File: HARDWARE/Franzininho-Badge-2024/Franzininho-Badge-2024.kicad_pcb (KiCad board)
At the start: 2 copper layers, 96 x 64 mm, 15 parts, among them SW1 SW_Push, U1 CH32V003F4P6

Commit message: Esboço inicial do layout.
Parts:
- added C4: 100nF, Capacitor_SMD:C_0603_1608Metric_Pad1.08x0.95mm_HandSolder, F.Cu at (112.1, 88.5)
- added C5: 10uF, Capacitor_SMD:C_0805_2012Metric_Pad1.18x1.45mm_HandSolder, F.Cu at (128.9, 81.7)
- added C6: 100nF, Capacitor_SMD:C_0603_1608Metric_Pad1.08x0.95mm_HandSolder, F.Cu at (128.7, 84.5)
- added J1: Conn_01x03_Pin, Connector_PinHeader_2.54mm:PinHeader_1x03_P2.54mm_Horizontal, F.Cu at (177.2, 105.4)
- added J2: Conn_01x04_Pin, Connector_PinHeader_2.54mm:PinHeader_1x04_P2.54mm_Horizontal, F.Cu at (177.2, 92.7)
- added R10: 1K, Resistor_SMD:R_0603_1608Metric_Pad0.98x0.95mm_HandSolder, F.Cu at (145.5, 105.4)
- added R11: 1K, Resistor_SMD:R_0603_1608Metric_Pad0.98x0.95mm_HandSolder, F.Cu at (128.5, 97.3)
- added R12: 1K, Resistor_SMD:R_0603_1608Metric_Pad0.98x0.95mm_HandSolder, F.Cu at (128.5, 98.8)
- added R13: 1K, Resistor_SMD:R_0603_1608Metric_Pad0.98x0.95mm_HandSolder, F.Cu at (145.5, 103.9)
- added R3: 1K, Resistor_SMD:R_0603_1608Metric_Pad0.98x0.95mm_HandSolder, F.Cu at (131.8, 97.3)
- added R4: 1K, Resistor_SMD:R_0603_1608Metric_Pad0.98x0.95mm_HandSolder, F.Cu at (131.8, 98.8)
- added R5: 1K, Resistor_SMD:R_0603_1608Metric_Pad0.98x0.95mm_HandSolder, F.Cu at (131.8, 100.8)
- added R6: 1K, Resistor_SMD:R_0603_1608Metric_Pad0.98x0.95mm_HandSolder, F.Cu at (131.8, 102.4)
- added R7: 1K, Resistor_SMD:R_0603_1608Metric_Pad0.98x0.95mm_HandSolder, F.Cu at (131.8, 103.9)
- added R8: 1K, Resistor_SMD:R_0603_1608Metric_Pad0.98x0.95mm_HandSolder, F.Cu at (131.8, 105.4)
- added R9: 1K, Resistor_SMD:R_0603_1608Metric_Pad0.98x0.95mm_HandSolder, F.Cu at (131.8, 106.9)
- added U2: OLED 128x64 1.3", Franzininho-Badge:OLED 128x64 1.3in, B.Cu at (139.7, 88.9)
- added U3: ~, Franzininho-Badge:EPAPER_1.54in_200x200, B.Cu at (139.7, 101.6)
- moved C2 15.4 mm to (146.3, 100.0), turned to -90 degrees
- moved C3 11.7 mm to (144.5, 100.0), turned to 90 degrees
- moved U1 1.63 mm to (139.7, 101.6), turned to 180 degrees
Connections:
- U1 pad 1: unconnected-(U1-PD4-Pad1) -> Net-(U1-PD4)
- U1 pad 11: unconnected-(U1-PC1-Pad11) -> Net-(U1-PC1)
- U1 pad 12: unconnected-(U1-PC2-Pad12) -> Net-(U1-PC2)
- U1 pad 15: unconnected-(U1-PC5-Pad15) -> Net-(U1-PC5)
- U1 pad 16: unconnected-(U1-PC6-Pad16) -> Net-(U1-PC6)
- U1 pad 18: unconnected-(U1-PD1-Pad18) -> Net-(U1-PD1)
- U1 pad 19: unconnected-(U1-PD2-Pad19) -> Net-(U1-PD2)
- U1 pad 2: unconnected-(U1-PD5-Pad2) -> Net-(U1-PD5)
- U1 pad 20: unconnected-(U1-PD3-Pad20) -> Net-(U1-PD3)
- U1 pad 3: unconnected-(U1-PD6-Pad3) -> MCU RX
- U1 pad 8: unconnected-(U1-PD0-Pad8) -> EPD BUSY
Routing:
- net SWIO: track 0.00 -> 48.1 mm
- net EPD BUSY: track 0.00 -> 41.8 mm
- net MCU RX: track 0.00 -> 37.9 mm
- net MCU TX: track 0.00 -> 33.2 mm
- net EPD RES: track 0.00 -> 24.3 mm
- net EPD D/C: track 0.00 -> 21.5 mm
- net SPI SCK: track 0.00 -> 15.6 mm
- net I2C SCL: track 0.00 -> 14.9 mm
- net SPI MOSI: track 0.00 -> 12.4 mm
- net I2C SDA: track 0.00 -> 11.9 mm
- net Net-(U1-PD3): track 0.00 -> 5.10 mm
- net Net-(U1-PD2): track 0.00 -> 4.73 mm
- net Net-(U1-PC1): track 0.00 -> 4.68 mm
- net Net-(U1-PD1): track 0.00 -> 4.37 mm
- net Net-(U1-PC2): track 0.00 -> 4.31 mm
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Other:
- board text added: "FRANZININHO BADGE 2024"

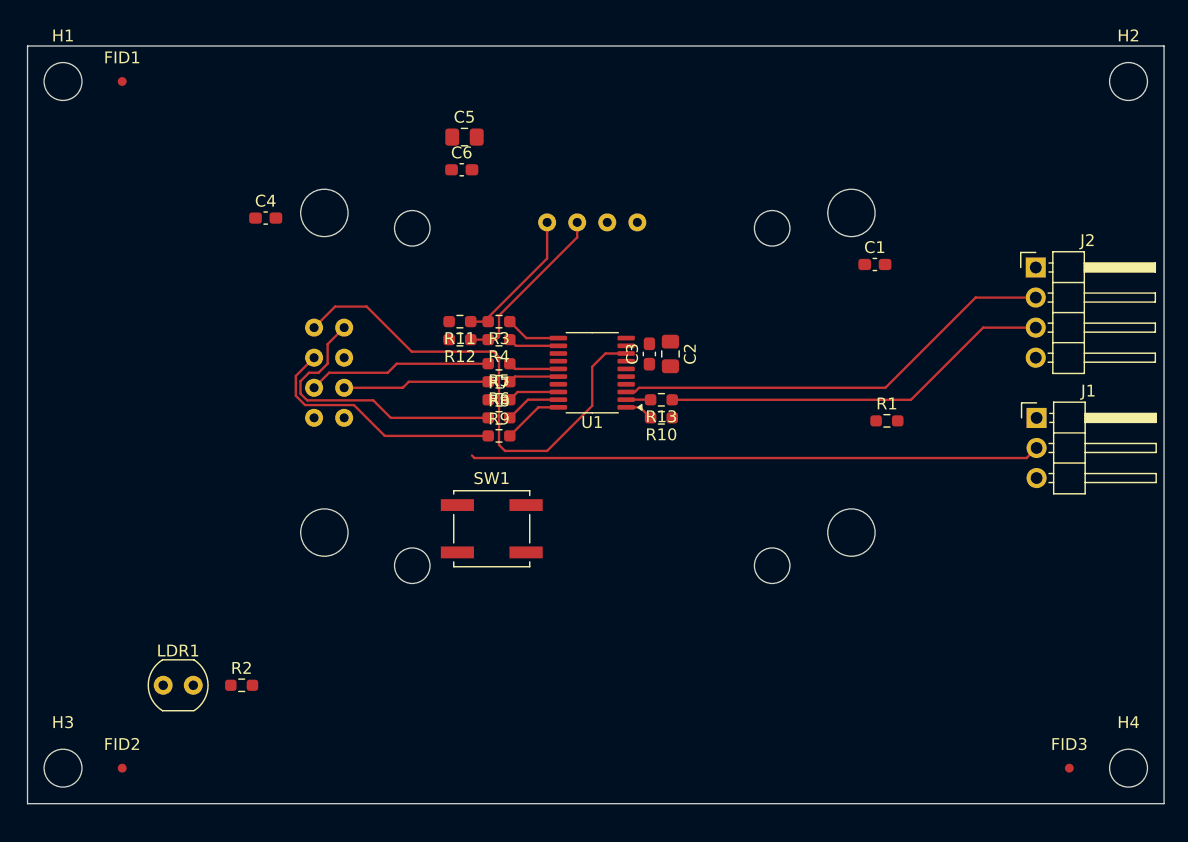
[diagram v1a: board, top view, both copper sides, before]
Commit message: Adicionado display de 2.13in; continuação do layout.
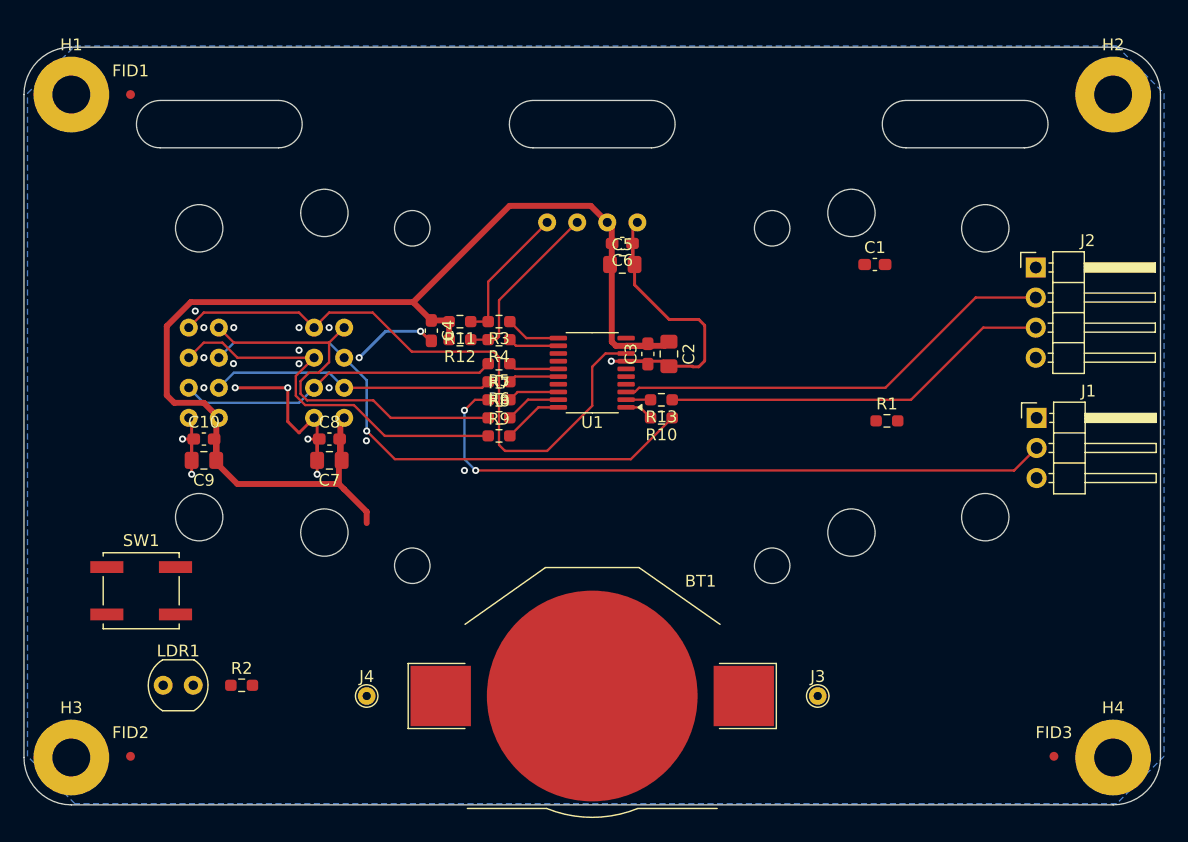
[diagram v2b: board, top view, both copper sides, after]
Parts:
- added BT1: CR2032, Battery:BatteryHolder_Keystone_3002_1x2032, F.Cu at (139.7, 128.9)
- added C10: 100nF, Capacitor_SMD:C_0603_1608Metric_Pad1.08x0.95mm_HandSolder, F.Cu at (106.9, 107.2)
- added C7: 10uF, Capacitor_SMD:C_0805_2012Metric_Pad1.18x1.45mm_HandSolder, F.Cu at (117.5, 109.0)
- added C8: 100nF, Capacitor_SMD:C_0603_1608Metric_Pad1.08x0.95mm_HandSolder, F.Cu at (117.5, 107.2)
- added C9: 10uF, Capacitor_SMD:C_0805_2012Metric_Pad1.18x1.45mm_HandSolder, F.Cu at (106.9, 109.0)
- added J3: +3V3, TestPoint:TestPoint_THTPad_D1.5mm_Drill0.7mm, F.Cu at (158.8, 128.9)
- added J4: GND, TestPoint:TestPoint_THTPad_D1.5mm_Drill0.7mm, F.Cu at (120.7, 128.9)
- added U4: 2.13in 250x122, Franzininho-Badge:EPAPER_2.13in_250x122, B.Cu at (139.7, 101.6)
- H1, H2, H3, H4: value MountingHole -> MountingHole_Pad; footprint MountingHole:MountingHole_3.2mm_M3_ISO7380 -> MountingHole:MountingHole_3.2mm_M3_Pad
- U3: value ~ -> 1.54in 200x200
- moved SW1 30.1 mm to (101.6, 120.0)
- moved C5 17.1 mm to (142.2, 92.5)
- moved C4 16.9 mm to (126.1, 98.0), turned to -90 degrees
- moved C6 14.9 mm to (142.2, 90.7), turned to 180 degrees
- moved H2 1.70 mm to (183.7, 78.1)
- moved FID3 1.64 mm to (178.7, 134.0)
- moved H4 1.58 mm to (183.7, 134.1)
- moved FID1 1.30 mm to (100.7, 78.1)
- moved H1 1.30 mm to (95.7, 78.1)
- moved FID2 1.22 mm to (100.7, 134.0)
- moved H3 1.14 mm to (95.7, 134.1)
- moved C2 0.13 mm to (146.2, 100.0)
- moved C3 0.13 mm to (144.4, 100.0)
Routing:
- net +3V3: track 0.00 -> 104.3 mm
- net GND: track 0.00 -> 61.1 mm, vias 0 -> 22
- net EPD CS: track 0.00 -> 46.9 mm, vias 0 -> 1
- net SPI SCK: track 15.6 -> 27.2 mm
- net SPI MOSI: track 12.4 -> 24.0 mm
- net EPD D/C: track 21.5 -> 33.1 mm
- net EPD BUSY: track 41.8 -> 53.0 mm
- net EPD RES: track 24.3 -> 34.1 mm
- net SWIO: track 48.1 -> 56.0 mm, vias 0 -> 2
- added copper zone on B.Cu, net GND
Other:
- outline, holes or cut-outs redrawn

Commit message: Adicionado circuito liga-desliga; finalizando layout.
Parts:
- removed the C1 at (163.6, 92.5)
- removed LDR1: VT93xx, OptoDevice:R_LDR_4.9x4.2mm_P2.54mm_Vertical
- removed R2: 1K, Resistor_SMD:R_0603_1608Metric_Pad0.98x0.95mm_HandSolder
- added C12: 100nF, Capacitor_SMD:C_0603_1608Metric_Pad1.08x0.95mm_HandSolder, F.Cu at (148.0, 101.3)
- added C3: 10uF, Capacitor_SMD:C_0805_2012Metric_Pad1.18x1.45mm_HandSolder, F.Cu at (168.6, 128.0)
- added G***: LOGO, LOGO, F.Cu at (110.8, 127.3)
- added G***: LOGO, LOGO, B.Cu at (139.7, 129.5)
- added Q1: SIL2308, Package_TO_SOT_SMD:SOT-23-6_Handsoldering, F.Cu at (165.1, 127.3)
- added R15: 1K, Resistor_SMD:R_0603_1608Metric_Pad0.98x0.95mm_HandSolder, F.Cu at (147.0, 97.2)
- added R16: 100K, Resistor_SMD:R_0603_1608Metric_Pad0.98x0.95mm_HandSolder, F.Cu at (101.9, 97.5)
- added R17: 100K, Resistor_SMD:R_0603_1608Metric_Pad0.98x0.95mm_HandSolder, F.Cu at (181.0, 125.7)
- added SW2: USER, Button_Switch_SMD:SW_Push_1P1T_NO_CK_KSC6xxJ, F.Cu at (98.1, 101.6)
- added SW3: RESET, Button_Switch_SMD:SW_Push_1P1T_NO_CK_KSC6xxJ, F.Cu at (177.2, 121.6)
- added TP3: +3V, TestPoint:TestPoint_THTPad_D1.5mm_Drill0.7mm, F.Cu at (171.4, 127.3)
- R1: value 1K -> 100K
- SW1: value SW_Push -> ON/OFF
- TP1: renamed from J3; value +3V3 -> +VBAT
- moved SW1 63.5 mm to (165.1, 121.6), turned to 0 degrees
- moved R1 22.8 mm to (161.6, 128.2), turned to 90 degrees
- moved TP2 1.91 mm to (120.7, 127.0)
- moved BT1 1.59 mm to (139.7, 127.3)
- moved TP1 1.59 mm to (158.8, 127.3)
- moved R7 1.49 mm to (147.0, 105.7)
- moved R8 1.48 mm to (147.0, 104.1)
- moved R10 0.57 mm to (132.4, 98.8)
- moved R11 0.57 mm to (132.4, 100.8)
- moved R12 0.57 mm to (132.4, 102.4)
- moved R4 0.57 mm to (132.4, 103.9)
- moved R5 0.57 mm to (132.4, 105.4)
- moved R6 0.57 mm to (132.4, 106.9)
- moved R9 0.57 mm to (132.4, 97.3)
- moved R13 0.38 mm to (128.9, 97.3)
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- renumbered C7 to C1, C5 to C10, C6 to C11, C8 to C2, C2 to C5, C3 to C6, C9 to C7, C10 to C8, C4 to C9, R4 to R10, R5 to R11, R6 to R12, R11 to R13, R12 to R14, R7 to R4, R8 to R5, R9 to R6, R10 to R7, R13 to R8, R3 to R9, J4 to TP2, U3 to U1, U1 to U2, U4 to U3, U2 to U4
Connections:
- net MCU RX renamed UART RX
- net MCU TX renamed UART TX
- net Net-(U1-PC1) renamed /MCU I2C SDA
- net Net-(U1-PC2) renamed /MCU I2C SCL
- net Net-(U1-PC5) renamed /MCU SPI SCK
- net Net-(U1-PC6) renamed /MCU SPI MOSI
- net Net-(U1-PD2) renamed /MCU EPD  RES
- net Net-(U1-PD3) renamed /MCU EPD D/~{C}
- net Net-(U1-PD4) renamed /MCU SPI ~{CS}
- net Net-(U1-PD5) renamed /MCU UART TX
- BT1 pad 1: +3V3 -> +VBAT
- C1 pad 1: +3V3 -> +3V
- C10 pad 1: +3V3 -> +3V
- C11 pad 2: +3V3 -> +3V
- C2 pad 2: +3V3 -> +3V
- C5 pad 1: +3V3 -> +3V
- C6 pad 2: +3V3 -> +3V
- C7 pad 1: +3V3 -> +3V
- C8 pad 2: +3V3 -> +3V
- C9 pad 1: +3V3 -> +3V
- J1 pad 1: +3V3 -> +3V
- J2 pad 1: +3V3 -> +3V
- R1 pad 1: unconnected-(R1-Pad1) -> Net-(Q1A-D1)
- R1 pad 2: unconnected-(R1-Pad2) -> +VBAT
- R13 pad 2: +3V3 -> +3V
- R14 pad 2: +3V3 -> +3V
- SW1 pad 1: unconnected-(SW1-Pad1) -> GND
- SW1 pad 2: unconnected-(SW1-Pad2) -> Net-(Q1A-D1)
- TP1 pad 1: +3V3 -> +VBAT
- U1 pad 8: +3V3 -> +3V
- U2 pad 10: unconnected-(U1-PC0-Pad10) -> Net-(U2-PC0)
- U2 pad 13: unconnected-(U1-PC3-Pad13) -> USER BUTTON
- U2 pad 4: unconnected-(U1-NRST/PD7-Pad4) -> ~{RESET}
- U2 pad 9: +3V3 -> +3V
- U3 pad 8: +3V3 -> +3V
- U4 pad 2: +3V3 -> +3V
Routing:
- net +3V: track 0.00 -> 196.8 mm
- net +3V3: track 104.3 -> 0.00 mm
- net GND: track 61.1 -> 141.2 mm, vias 22 -> 60
- net ~{RESET}: track 0.00 -> 57.6 mm, vias 0 -> 2
- net USER BUTTON: track 0.00 -> 51.5 mm, vias 0 -> 2
- net +VBAT: track 0.00 -> 50.4 mm
- net ~{SHUTDOWN}: track 0.00 -> 39.1 mm, vias 0 -> 2
- net Net-(Q1A-D1): track 0.00 -> 16.5 mm
- net Net-(U2-PC0): track 0.00 -> 4.16 mm
- net EPD RES: track 34.1 -> 36.5 mm
- net /MCU SPI ~{CS}: track 2.43 -> 4.03 mm
- net /MCU UART TX: track 2.07 -> 3.64 mm
- net UART TX: track 33.2 -> 31.9 mm
- net EPD CS: track 46.9 -> 48.2 mm
- net SWIO: track 56.0 -> 55.1 mm
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- added copper zone on F.Cu, net GND
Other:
- board text added: "BADGE 2024 REV. 00 2024.05.25"
- board text removed: "FRANZININHO BADGE 2024"

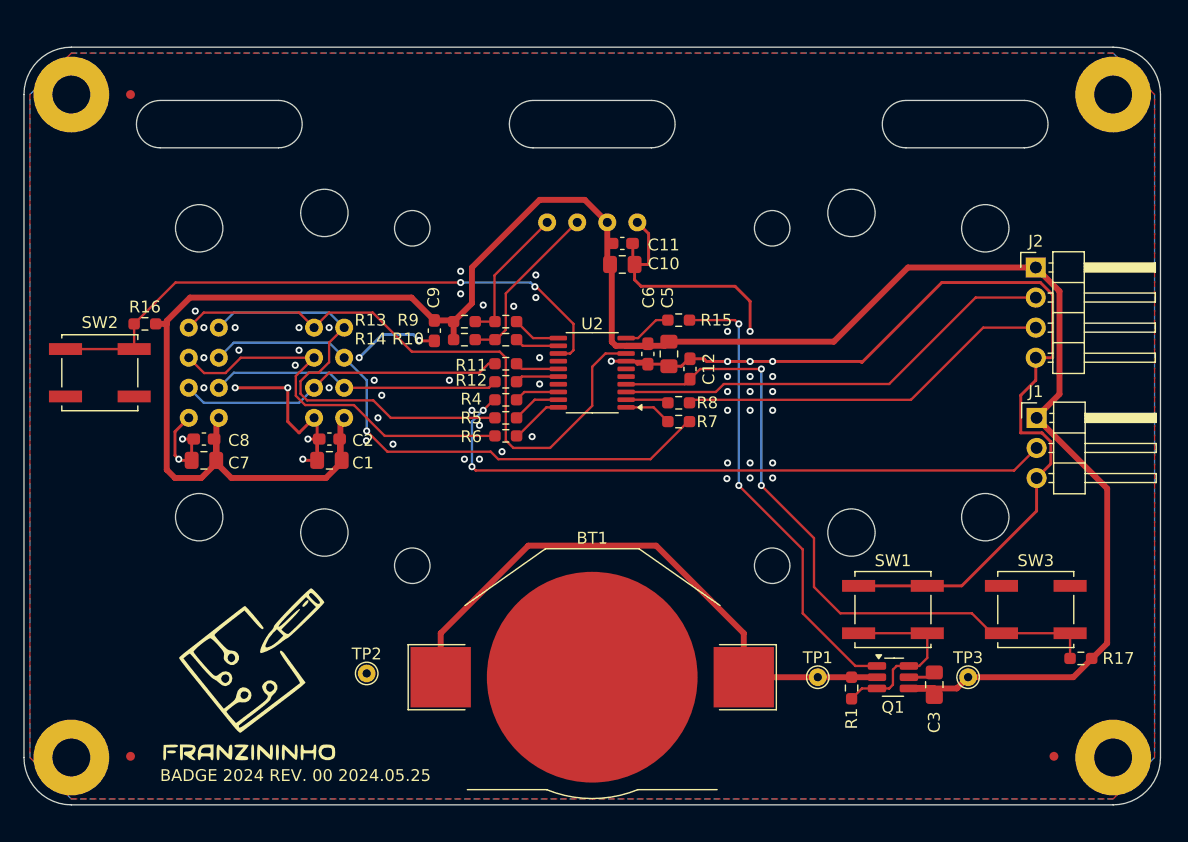
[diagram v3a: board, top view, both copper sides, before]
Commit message: Finalização do projeto; adicionados test points e LEDs; adicionado conector para SPI; ajuste nas marcações; renumeração; ajustes no layout.
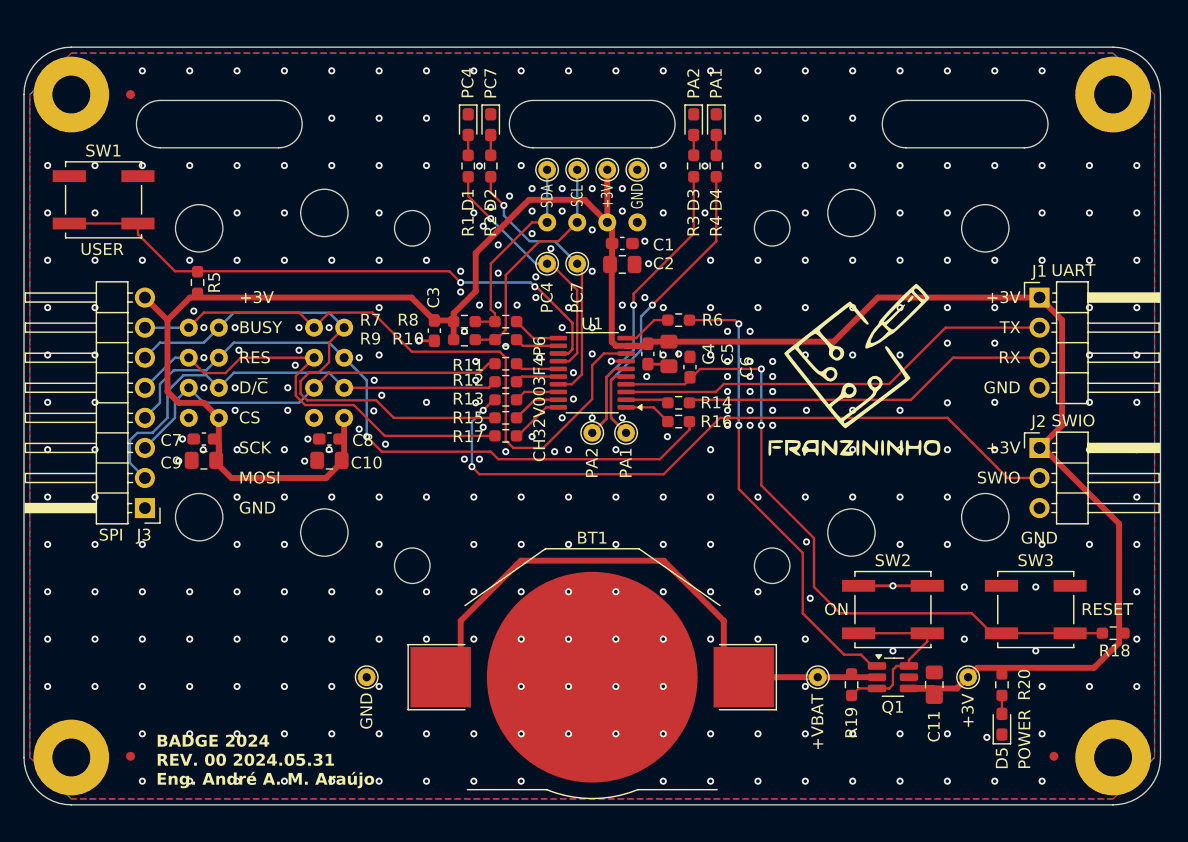
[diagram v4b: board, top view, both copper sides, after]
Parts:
- removed the U1 at (139.7, 101.6)
- added D1: PC4, LED_SMD:LED_0603_1608Metric_Pad1.05x0.95mm_HandSolder, F.Cu at (129.2, 80.6)
- added D2: PC7, LED_SMD:LED_0603_1608Metric_Pad1.05x0.95mm_HandSolder, F.Cu at (131.1, 80.6)
- added D3: PA2, LED_SMD:LED_0603_1608Metric_Pad1.05x0.95mm_HandSolder, F.Cu at (148.3, 80.6)
- added D4: PA1, LED_SMD:LED_0603_1608Metric_Pad1.05x0.95mm_HandSolder, F.Cu at (150.2, 80.6)
- added D5: POWER, LED_SMD:LED_0603_1608Metric_Pad1.05x0.95mm_HandSolder, F.Cu at (174.3, 131.3)
- added J3: SPI, Connector_PinHeader_2.54mm:PinHeader_1x08_P2.54mm_Horizontal, F.Cu at (101.9, 113.0)
- added R1: 1K, Resistor_SMD:R_0603_1608Metric_Pad0.98x0.95mm_HandSolder, F.Cu at (129.2, 84.1)
- added R2: 1K, Resistor_SMD:R_0603_1608Metric_Pad0.98x0.95mm_HandSolder, F.Cu at (131.1, 84.1)
- added R20: 1K, Resistor_SMD:R_0603_1608Metric_Pad0.98x0.95mm_HandSolder, F.Cu at (174.3, 128.0)
- added R3: 1K, Resistor_SMD:R_0603_1608Metric_Pad0.98x0.95mm_HandSolder, F.Cu at (148.3, 84.1)
- added R4: 1K, Resistor_SMD:R_0603_1608Metric_Pad0.98x0.95mm_HandSolder, F.Cu at (150.2, 84.1)
- added TP1: SDA, TestPoint:TestPoint_THTPad_D1.5mm_Drill0.7mm, F.Cu at (135.9, 84.5)
- added TP2: SCL, TestPoint:TestPoint_THTPad_D1.5mm_Drill0.7mm, F.Cu at (138.4, 84.5)
- added TP3: +3V, TestPoint:TestPoint_THTPad_D1.5mm_Drill0.7mm, F.Cu at (141.0, 84.5)
- added TP4: GND, TestPoint:TestPoint_THTPad_D1.5mm_Drill0.7mm, F.Cu at (143.5, 84.5)
- added TP5: PC4, TestPoint:TestPoint_THTPad_D1.5mm_Drill0.7mm, F.Cu at (135.9, 92.4)
- added TP6: PC7, TestPoint:TestPoint_THTPad_D1.5mm_Drill0.7mm, F.Cu at (138.4, 92.4)
- added TP7: PA2, TestPoint:TestPoint_THTPad_D1.5mm_Drill0.7mm, F.Cu at (139.7, 106.7)
- added TP8: PA1, TestPoint:TestPoint_THTPad_D1.5mm_Drill0.7mm, F.Cu at (142.6, 106.7)
- added U3: 1.54in 200x200, Franzininho-Badge:EPAPER_1.54in_200x200, B.Cu at (139.7, 101.6)
- J1: renamed from J2; value Conn_01x04_Pin -> UART
- J2: renamed from J1; value Conn_01x03_Pin -> SWIO
- SW2: renamed from SW1; value ON/OFF -> ON
- moved G*** 60.4 mm to (182.2, 86.6)
- moved G*** 57.2 mm to (161.9, 101.6)
- moved SW1 14.6 mm to (98.4, 87.0), turned to 0 degrees
- moved R5 5.65 mm to (106.4, 94.0), turned to -90 degrees
- moved R18 3.46 mm to (183.7, 123.6)
- moved J1 2.56 mm to (177.5, 95.2)
- moved J2 2.55 mm to (177.5, 108.0)
- moved TP9 0.32 mm to (120.7, 127.3)
- moved R19 0.28 mm to (161.6, 128.0)
- moved C6 0.16 mm to (148.0, 101.1)
- renumbered C11 to C1, C1 to C10, C3 to C11, C10 to C2, C9 to C3, C6 to C4, C12 to C6, C8 to C7, C2 to C8, C7 to C9, R4 to R13, R8 to R14, R5 to R15, R7 to R16, R6 to R17, R17 to R18, R1 to R19, R16 to R5, R15 to R6, R13 to R7, R9 to R8, R14 to R9, SW2 to SW1, TP1 to TP10, TP3 to TP11, TP2 to TP9, U2 to U1, U4 to U2, U3 to U4
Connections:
- net Net-(U2-PC0) renamed /MCU ~{SHUTDOWN}
- net Net-(U2-PD1) renamed /MCU SWIO
- U1 pad 14: unconnected-(U2-PC4-Pad14) -> /MCU PC4
- U1 pad 17: unconnected-(U2-PC7-Pad17) -> /MCU PC7
- U1 pad 5: unconnected-(U2-OSC_IN/PA1-Pad5) -> /MCU PA1
- U1 pad 6: unconnected-(U2-OSC_OUT/PA2-Pad6) -> /MCU PA2
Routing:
- net GND: track 141.2 -> 11.7 mm, vias 60 -> 360
- net /MCU PA2: track 0.00 -> 32.3 mm, vias 0 -> 1
- net /MCU PA1: track 0.00 -> 32.2 mm, vias 0 -> 1
- net /MCU PC7: track 0.00 -> 23.5 mm, vias 0 -> 1
- net /MCU PC4: track 0.00 -> 21.3 mm, vias 0 -> 1
- net SPI MOSI: track 24.6 -> 39.8 mm
- net EPD CS: track 48.2 -> 58.1 mm
- net EPD RES: track 36.5 -> 43.8 mm
- net SPI SCK: track 27.8 -> 34.4 mm
- net +3V: track 196.8 -> 191.1 mm
- net I2C SDA: track 11.9 -> 16.7 mm
- net EPD D/C: track 33.7 -> 38.5 mm
- net I2C SCL: track 14.5 -> 19.2 mm
- net SWIO: track 55.1 -> 58.8 mm
- net EPD BUSY: track 52.6 -> 56.0 mm
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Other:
- board text added: "+3V"
- board text added: "BADGE 2024 REV. 00 2024.05.31 Eng. André A. M. Araújo"
- board text added: "BUSY"
- board text added: "CS"
- board text added: "D/~{C}"
- board text added: "GND"
- board text added: "MOSI"
- board text added: "RES"
- board text added: "RX"
- board text added: "SCK"
- board text added: "SWIO"
- board text added: "TX"
- board text removed: "BADGE 2024 REV. 00 2024.05.25"
